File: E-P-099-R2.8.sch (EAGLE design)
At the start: 86 parts, among them J1 AVR_ISP

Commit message: pinouts updated to match new light boards
New changes to the pinouts for the ethernet connectors to match the new design of the head and tail light boards. Also designed to be symmetric across the connector to prevent mistakes.
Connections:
- removed net N$20: FRONT.1, U$20.D
- removed net N$23: FRONT.3, U$11.D
- new net N$14: FRONT.2, U$20.D
- new net N$15: FRONT.7, U$11.D
- net +12V: now also FRONT.3, FRONT.6, REAR.4, REAR.6; no longer FRONT.2, FRONT.7, REAR.1, REAR.2
- net N$27: now also FRONT.1; no longer FRONT.6
- net N$4: now also REAR.1; no longer REAR.7
- net N$43: now also REAR.7; no longer REAR.4
- net N$5: now also REAR.2; no longer REAR.6
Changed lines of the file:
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@@
 <instance part="R8" gate="G$1" x="111.76" y="226.06" rot="R90"/>
 <instance part="LED12" gate="G$1" x="111.76" y="236.22"/>
-<instance part="P+2" gate="1" x="45.72" y="27.94" rot="R180"/>
+<instance part="P+2" gate="1" x="43.18" y="27.94" rot="R180"/>
 <instance part="U$1" gate="G$1" x="408.94" y="144.78" rot="R90"/>
 <instance part="U$2" gate="G$1" x="391.16" y="129.54" rot="MR0"/>
@@
 <segment>
 <pinref part="P+6" gate="1" pin="+12V"/>
-<wire x1="53.34" y1="266.7" x2="53.34" y2="259.08" width="0.1524" layer="91"/>
-<wire x1="53.34" y1="259.08" x2="53.34" y2="254" width="0.1524" layer="91"/>
-<wire x1="53.34" y1="254" x2="53.34" y2="251.46" width="0.1524" layer="91"/>
-<wire x1="53.34" y1="251.46" x2="53.34" y2="246.38" width="0.1524" layer="91"/>
-<wire x1="53.34" y1="246.38" x2="60.96" y2="246.38" width="0.1524" layer="91"/>
-<wire x1="60.96" y1="251.46" x2="53.34" y2="251.46" width="0.1524" layer="91"/>
-<junction x="53.34" y="251.46"/>
-<wire x1="53.34" y1="254" x2="60.96" y2="254" width="0.1524" layer="91"/>
-<junction x="53.34" y="254"/>
-<wire x1="53.34" y1="259.08" x2="60.96" y2="259.08" width="0.1524" layer="91"/>
-<junction x="53.34" y="259.08"/>
-<pinref part="FRONT" gate="G$1" pin="2"/>
+<wire x1="53.34" y1="266.7" x2="53.34" y2="256.54" width="0.1524" layer="91"/>
+<pinref part="FRONT" gate="G$1" pin="6"/>
+<pinref part="FRONT" gate="G$1" pin="5"/>
+<wire x1="60.96" y1="248.92" x2="60.96" y2="251.46" width="0.1524" layer="91"/>
 <pinref part="FRONT" gate="G$1" pin="4"/>
-<pinref part="FRONT" gate="G$1" pin="5"/>
-<pinref part="FRONT" gate="G$1" pin="7"/>
-</segment>
-<segment>
+<wire x1="60.96" y1="251.46" x2="60.96" y2="254" width="0.1524" layer="91"/>
+<junction x="60.96" y="251.46"/>
+<pinref part="FRONT" gate="G$1" pin="3"/>
+<wire x1="60.96" y1="254" x2="60.96" y2="256.54" width="0.1524" layer="91"/>
+<junction x="60.96" y="254"/>
+<wire x1="60.96" y1="256.54" x2="53.34" y2="256.54" width="0.1524" layer="91"/>
+<junction x="60.96" y="256.54"/>
+</segment>
+<segment>
+<pinref part="REAR" gate="G$1" pin="6"/>
+<pinref part="REAR" gate="G$1" pin="5"/>
+<wire x1="43.18" y1="45.72" x2="43.18" y2="43.18" width="0.1524" layer="91"/>
+<pinref part="REAR" gate="G$1" pin="4"/>
+<wire x1="43.18" y1="43.18" x2="43.18" y2="40.64" width="0.1524" layer="91"/>
+<junction x="43.18" y="43.18"/>
+<pinref part="REAR" gate="G$1" pin="3"/>
+<wire x1="43.18" y1="40.64" x2="43.18" y2="38.1" width="0.1524" layer="91"/>
+<junction x="43.18" y="40.64"/>
+<wire x1="43.18" y1="38.1" x2="43.18" y2="30.48" width="0.1524" layer="91"/>
+<junction x="43.18" y="38.1"/>
 <pinref part="P+2" gate="1" pin="+12V"/>
-<wire x1="45.72" y1="30.48" x2="45.72" y2="33.02" width="0.1524" layer="91"/>
-<wire x1="45.72" y1="33.02" x2="45.72" y2="35.56" width="0.1524" layer="91"/>
-<wire x1="45.72" y1="35.56" x2="45.72" y2="38.1" width="0.1524" layer="91"/>
-<pinref part="REAR" gate="G$1" pin="3"/>
-<wire x1="43.18" y1="38.1" x2="45.72" y2="38.1" width="0.1524" layer="91"/>
-<pinref part="REAR" gate="G$1" pin="2"/>
-<wire x1="43.18" y1="35.56" x2="45.72" y2="35.56" width="0.1524" layer="91"/>
-<junction x="45.72" y="35.56"/>
-<pinref part="REAR" gate="G$1" pin="1"/>
-<wire x1="43.18" y1="33.02" x2="45.72" y2="33.02" width="0.1524" layer="91"/>
-<junction x="45.72" y="33.02"/>
-<wire x1="45.72" y1="38.1" x2="45.72" y2="43.18" width="0.1524" layer="91"/>
-<junction x="45.72" y="38.1"/>
-<pinref part="REAR" gate="G$1" pin="5"/>
-<wire x1="45.72" y1="43.18" x2="43.18" y2="43.18" width="0.1524" layer="91"/>
 </segment>
 </net>
 <net name="N$43" class="0">
 <segment>
-<wire x1="91.44" y1="40.64" x2="91.44" y2="60.96" width="0.1524" layer="91"/>
+<wire x1="91.44" y1="48.26" x2="91.44" y2="60.96" width="0.1524" layer="91"/>
 <wire x1="91.44" y1="60.96" x2="119.38" y2="60.96" width="0.1524" layer="91"/>
 <wire x1="119.38" y1="60.96" x2="119.38" y2="55.88" width="0.1524" layer="91"/>
 <pinref part="U$14" gate="G$1" pin="D"/>
-<pinref part="REAR" gate="G$1" pin="4"/>
-<wire x1="43.18" y1="40.64" x2="91.44" y2="40.64" width="0.1524" layer="91"/>
+<pinref part="REAR" gate="G$1" pin="7"/>
+<wire x1="43.18" y1="48.26" x2="91.44" y2="48.26" width="0.1524" layer="91"/>
 </segment>
 </net>
@@
 </segment>
 </net>
-<net name="N$20" class="0">
-<segment>
-<wire x1="40.64" y1="256.54" x2="40.64" y2="261.62" width="0.1524" layer="91"/>
-<wire x1="40.64" y1="261.62" x2="60.96" y2="261.62" width="0.1524" layer="91"/>
-<pinref part="U$20" gate="G$1" pin="D"/>
-<pinref part="FRONT" gate="G$1" pin="1"/>
-</segment>
-</net>
-<net name="N$23" class="0">
-<segment>
-<wire x1="45.72" y1="248.92" x2="45.72" y2="256.54" width="0.1524" layer="91"/>
-<wire x1="45.72" y1="256.54" x2="60.96" y2="256.54" width="0.1524" layer="91"/>
-<pinref part="U$11" gate="G$1" pin="D"/>
-<pinref part="FRONT" gate="G$1" pin="3"/>
-</segment>
-</net>
 <net name="N$27" class="0">
 <segment>
 <wire x1="50.8" y1="228.6" x2="50.8" y2="243.84" width="0.1524" layer="91"/>
 <wire x1="50.8" y1="243.84" x2="60.96" y2="243.84" width="0.1524" layer="91"/>
-<wire x1="50.8" y1="243.84" x2="50.8" y2="248.92" width="0.1524" layer="91"/>
+<pinref part="U$10" gate="G$1" pin="D"/>
+<pinref part="FRONT" gate="G$1" pin="8"/>
+<wire x1="50.8" y1="243.84" x2="50.8" y2="261.62" width="0.1524" layer="91"/>
 <junction x="50.8" y="243.84"/>
-<wire x1="50.8" y1="248.92" x2="60.96" y2="248.92" width="0.1524" layer="91"/>
-<pinref part="U$10" gate="G$1" pin="D"/>
-<pinref part="FRONT" gate="G$1" pin="6"/>
-<pinref part="FRONT" gate="G$1" pin="8"/>
+<pinref part="FRONT" gate="G$1" pin="1"/>
+<wire x1="50.8" y1="261.62" x2="60.96" y2="261.62" width="0.1524" layer="91"/>
 </segment>
 </net>
@@
 <net name="N$4" class="0">
 <segment>
-<pinref part="REAR" gate="G$1" pin="7"/>
-<pinref part="REAR" gate="G$1" pin="8"/>
-<wire x1="43.18" y1="48.26" x2="43.18" y2="50.8" width="0.1524" layer="91"/>
 <pinref part="U$13" gate="G$1" pin="D"/>
 <wire x1="58.42" y1="81.28" x2="93.98" y2="81.28" width="0.1524" layer="91"/>
+<wire x1="58.42" y1="81.28" x2="58.42" y2="50.8" width="0.1524" layer="91"/>
+<pinref part="REAR" gate="G$1" pin="1"/>
+<wire x1="58.42" y1="50.8" x2="58.42" y2="33.02" width="0.1524" layer="91"/>
+<wire x1="58.42" y1="33.02" x2="43.18" y2="33.02" width="0.1524" layer="91"/>
+<pinref part="REAR" gate="G$1" pin="8"/>
 <wire x1="43.18" y1="50.8" x2="58.42" y2="50.8" width="0.1524" layer="91"/>
-<wire x1="58.42" y1="50.8" x2="58.42" y2="81.28" width="0.1524" layer="91"/>
-<junction x="43.18" y="50.8"/>
+<junction x="58.42" y="50.8"/>
 </segment>
 </net>
@@
 <segment>
 <pinref part="U$15" gate="G$1" pin="D"/>
-<wire x1="119.38" y1="25.4" x2="119.38" y2="30.48" width="0.1524" layer="91"/>
-<pinref part="REAR" gate="G$1" pin="6"/>
-<wire x1="43.18" y1="45.72" x2="58.42" y2="45.72" width="0.1524" layer="91"/>
-<wire x1="58.42" y1="45.72" x2="58.42" y2="25.4" width="0.1524" layer="91"/>
-<wire x1="58.42" y1="25.4" x2="119.38" y2="25.4" width="0.1524" layer="91"/>
+<pinref part="REAR" gate="G$1" pin="2"/>
+<wire x1="43.18" y1="35.56" x2="101.6" y2="35.56" width="0.1524" layer="91"/>
+<wire x1="101.6" y1="35.56" x2="101.6" y2="30.48" width="0.1524" layer="91"/>
+<wire x1="101.6" y1="30.48" x2="119.38" y2="30.48" width="0.1524" layer="91"/>
 </segment>
 </net>
@@
 </segment>
 </net>
+<net name="N$14" class="0">
+<segment>
+<pinref part="U$20" gate="G$1" pin="D"/>
+<wire x1="40.64" y1="256.54" x2="40.64" y2="259.08" width="0.1524" layer="91"/>
+<pinref part="FRONT" gate="G$1" pin="2"/>
+<wire x1="40.64" y1="259.08" x2="60.96" y2="259.08" width="0.1524" layer="91"/>
+</segment>
+</net>
+<net name="N$15" class="0">
+<segment>
+<pinref part="U$11" gate="G$1" pin="D"/>
+<wire x1="45.72" y1="248.92" x2="55.88" y2="248.92" width="0.1524" layer="91"/>
+<wire x1="55.88" y1="248.92" x2="55.88" y2="246.38" width="0.1524" layer="91"/>
+<pinref part="FRONT" gate="G$1" pin="7"/>
+<wire x1="55.88" y1="246.38" x2="60.96" y2="246.38" width="0.1524" layer="91"/>
+</segment>
+</net>

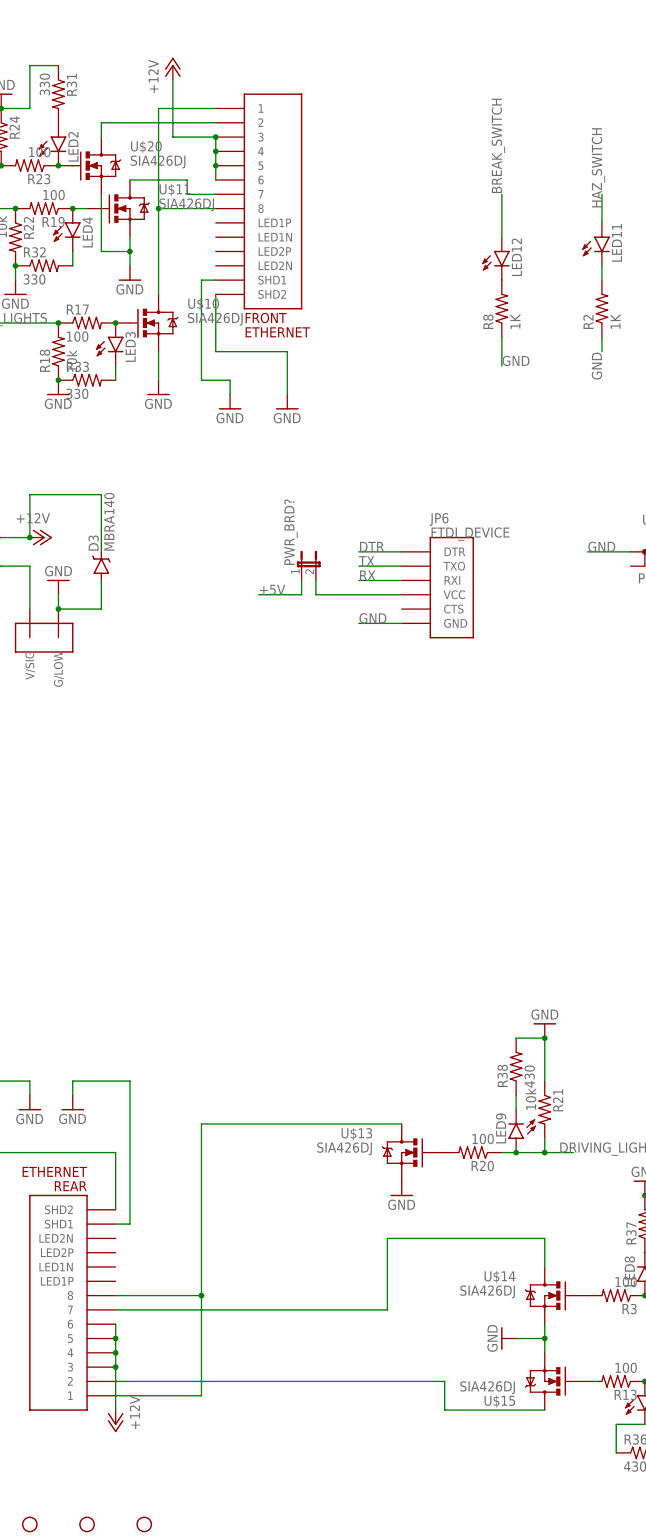
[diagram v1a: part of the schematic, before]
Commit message: Revert "pinouts updated to match new light boards"
This reverts commit c6705fe930e627c4a8d5c034fe7450b97c4f4bb6.
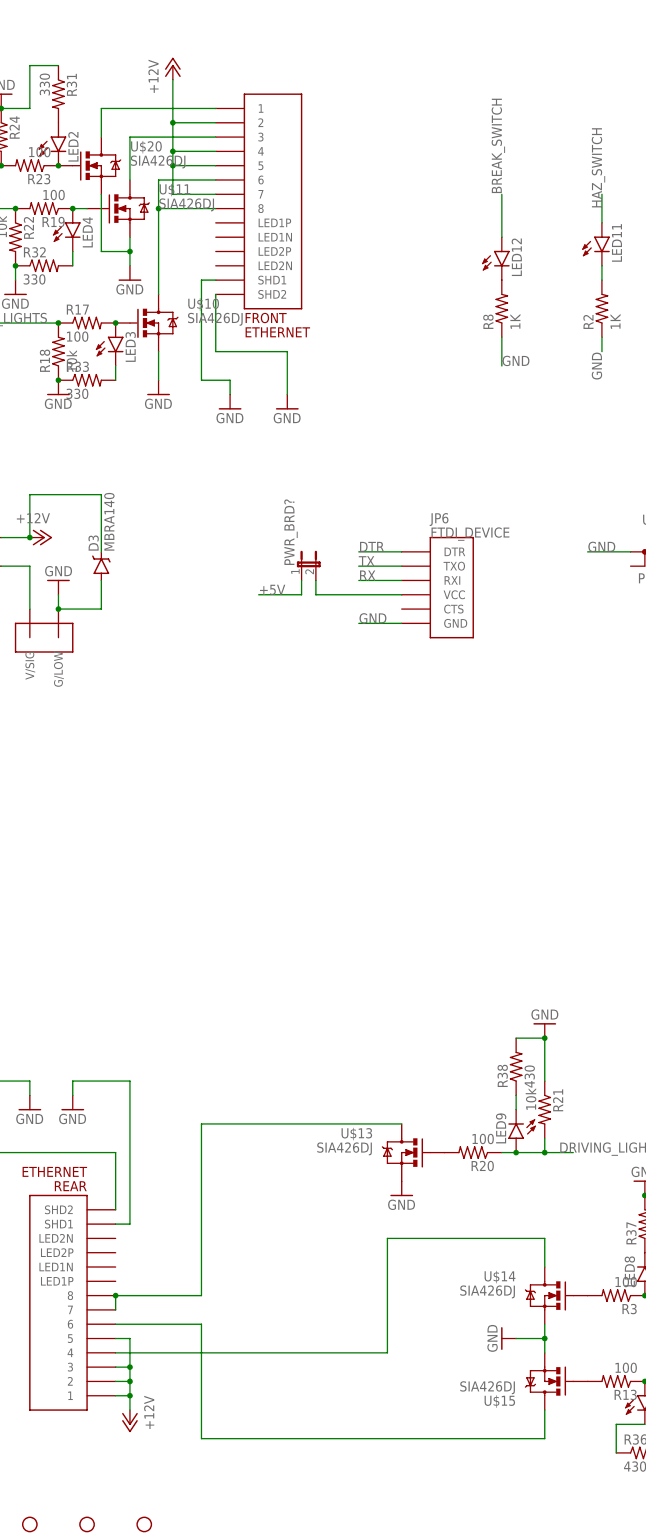
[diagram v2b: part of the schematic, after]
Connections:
- removed net N$14: FRONT.2, U$20.D
- removed net N$15: FRONT.7, U$11.D
- new net N$20: FRONT.1, U$20.D
- new net N$23: FRONT.3, U$11.D
- net +12V: now also FRONT.2, FRONT.7, REAR.1, REAR.2; no longer FRONT.3, FRONT.6, REAR.4, REAR.6
- net N$27: now also FRONT.6; no longer FRONT.1
- net N$4: now also REAR.7; no longer REAR.1
- net N$43: now also REAR.4; no longer REAR.7
- net N$5: now also REAR.6; no longer REAR.2
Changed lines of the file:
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@@
 <instance part="R8" gate="G$1" x="111.76" y="226.06" rot="R90"/>
 <instance part="LED12" gate="G$1" x="111.76" y="236.22"/>
-<instance part="P+2" gate="1" x="43.18" y="27.94" rot="R180"/>
+<instance part="P+2" gate="1" x="45.72" y="27.94" rot="R180"/>
 <instance part="U$1" gate="G$1" x="408.94" y="144.78" rot="R90"/>
 <instance part="U$2" gate="G$1" x="391.16" y="129.54" rot="MR0"/>
@@
 <segment>
 <pinref part="P+6" gate="1" pin="+12V"/>
-<wire x1="53.34" y1="266.7" x2="53.34" y2="256.54" width="0.1524" layer="91"/>
-<pinref part="FRONT" gate="G$1" pin="6"/>
+<wire x1="53.34" y1="266.7" x2="53.34" y2="259.08" width="0.1524" layer="91"/>
+<wire x1="53.34" y1="259.08" x2="53.34" y2="254" width="0.1524" layer="91"/>
+<wire x1="53.34" y1="254" x2="53.34" y2="251.46" width="0.1524" layer="91"/>
+<wire x1="53.34" y1="251.46" x2="53.34" y2="246.38" width="0.1524" layer="91"/>
+<wire x1="53.34" y1="246.38" x2="60.96" y2="246.38" width="0.1524" layer="91"/>
+<wire x1="60.96" y1="251.46" x2="53.34" y2="251.46" width="0.1524" layer="91"/>
+<junction x="53.34" y="251.46"/>
+<wire x1="53.34" y1="254" x2="60.96" y2="254" width="0.1524" layer="91"/>
+<junction x="53.34" y="254"/>
+<wire x1="53.34" y1="259.08" x2="60.96" y2="259.08" width="0.1524" layer="91"/>
+<junction x="53.34" y="259.08"/>
+<pinref part="FRONT" gate="G$1" pin="2"/>
+<pinref part="FRONT" gate="G$1" pin="4"/>
 <pinref part="FRONT" gate="G$1" pin="5"/>
-<wire x1="60.96" y1="248.92" x2="60.96" y2="251.46" width="0.1524" layer="91"/>
-<pinref part="FRONT" gate="G$1" pin="4"/>
-<wire x1="60.96" y1="251.46" x2="60.96" y2="254" width="0.1524" layer="91"/>
-<junction x="60.96" y="251.46"/>
-<pinref part="FRONT" gate="G$1" pin="3"/>
-<wire x1="60.96" y1="254" x2="60.96" y2="256.54" width="0.1524" layer="91"/>
-<junction x="60.96" y="254"/>
-<wire x1="60.96" y1="256.54" x2="53.34" y2="256.54" width="0.1524" layer="91"/>
-<junction x="60.96" y="256.54"/>
-</segment>
-<segment>
-<pinref part="REAR" gate="G$1" pin="6"/>
+<pinref part="FRONT" gate="G$1" pin="7"/>
+</segment>
+<segment>
+<pinref part="P+2" gate="1" pin="+12V"/>
+<wire x1="45.72" y1="30.48" x2="45.72" y2="33.02" width="0.1524" layer="91"/>
+<wire x1="45.72" y1="33.02" x2="45.72" y2="35.56" width="0.1524" layer="91"/>
+<wire x1="45.72" y1="35.56" x2="45.72" y2="38.1" width="0.1524" layer="91"/>
+<pinref part="REAR" gate="G$1" pin="3"/>
+<wire x1="43.18" y1="38.1" x2="45.72" y2="38.1" width="0.1524" layer="91"/>
+<pinref part="REAR" gate="G$1" pin="2"/>
+<wire x1="43.18" y1="35.56" x2="45.72" y2="35.56" width="0.1524" layer="91"/>
+<junction x="45.72" y="35.56"/>
+<pinref part="REAR" gate="G$1" pin="1"/>
+<wire x1="43.18" y1="33.02" x2="45.72" y2="33.02" width="0.1524" layer="91"/>
+<junction x="45.72" y="33.02"/>
+<wire x1="45.72" y1="38.1" x2="45.72" y2="43.18" width="0.1524" layer="91"/>
+<junction x="45.72" y="38.1"/>
 <pinref part="REAR" gate="G$1" pin="5"/>
-<wire x1="43.18" y1="45.72" x2="43.18" y2="43.18" width="0.1524" layer="91"/>
-<pinref part="REAR" gate="G$1" pin="4"/>
-<wire x1="43.18" y1="43.18" x2="43.18" y2="40.64" width="0.1524" layer="91"/>
-<junction x="43.18" y="43.18"/>
-<pinref part="REAR" gate="G$1" pin="3"/>
-<wire x1="43.18" y1="40.64" x2="43.18" y2="38.1" width="0.1524" layer="91"/>
-<junction x="43.18" y="40.64"/>
-<wire x1="43.18" y1="38.1" x2="43.18" y2="30.48" width="0.1524" layer="91"/>
-<junction x="43.18" y="38.1"/>
-<pinref part="P+2" gate="1" pin="+12V"/>
+<wire x1="45.72" y1="43.18" x2="43.18" y2="43.18" width="0.1524" layer="91"/>
 </segment>
 </net>
 <net name="N$43" class="0">
 <segment>
-<wire x1="91.44" y1="48.26" x2="91.44" y2="60.96" width="0.1524" layer="91"/>
+<wire x1="91.44" y1="40.64" x2="91.44" y2="60.96" width="0.1524" layer="91"/>
 <wire x1="91.44" y1="60.96" x2="119.38" y2="60.96" width="0.1524" layer="91"/>
 <wire x1="119.38" y1="60.96" x2="119.38" y2="55.88" width="0.1524" layer="91"/>
 <pinref part="U$14" gate="G$1" pin="D"/>
-<pinref part="REAR" gate="G$1" pin="7"/>
-<wire x1="43.18" y1="48.26" x2="91.44" y2="48.26" width="0.1524" layer="91"/>
+<pinref part="REAR" gate="G$1" pin="4"/>
+<wire x1="43.18" y1="40.64" x2="91.44" y2="40.64" width="0.1524" layer="91"/>
 </segment>
 </net>
@@
 </segment>
 </net>
+<net name="N$20" class="0">
+<segment>
+<wire x1="40.64" y1="256.54" x2="40.64" y2="261.62" width="0.1524" layer="91"/>
+<wire x1="40.64" y1="261.62" x2="60.96" y2="261.62" width="0.1524" layer="91"/>
+<pinref part="U$20" gate="G$1" pin="D"/>
+<pinref part="FRONT" gate="G$1" pin="1"/>
+</segment>
+</net>
+<net name="N$23" class="0">
+<segment>
+<wire x1="45.72" y1="248.92" x2="45.72" y2="256.54" width="0.1524" layer="91"/>
+<wire x1="45.72" y1="256.54" x2="60.96" y2="256.54" width="0.1524" layer="91"/>
+<pinref part="U$11" gate="G$1" pin="D"/>
+<pinref part="FRONT" gate="G$1" pin="3"/>
+</segment>
+</net>
 <net name="N$27" class="0">
 <segment>
 <wire x1="50.8" y1="228.6" x2="50.8" y2="243.84" width="0.1524" layer="91"/>
 <wire x1="50.8" y1="243.84" x2="60.96" y2="243.84" width="0.1524" layer="91"/>
+<wire x1="50.8" y1="243.84" x2="50.8" y2="248.92" width="0.1524" layer="91"/>
+<junction x="50.8" y="243.84"/>
+<wire x1="50.8" y1="248.92" x2="60.96" y2="248.92" width="0.1524" layer="91"/>
 <pinref part="U$10" gate="G$1" pin="D"/>
+<pinref part="FRONT" gate="G$1" pin="6"/>
 <pinref part="FRONT" gate="G$1" pin="8"/>
-<wire x1="50.8" y1="243.84" x2="50.8" y2="261.62" width="0.1524" layer="91"/>
-<junction x="50.8" y="243.84"/>
-<pinref part="FRONT" gate="G$1" pin="1"/>
-<wire x1="50.8" y1="261.62" x2="60.96" y2="261.62" width="0.1524" layer="91"/>
 </segment>
 </net>
@@
 <net name="N$4" class="0">
 <segment>
+<pinref part="REAR" gate="G$1" pin="7"/>
+<pinref part="REAR" gate="G$1" pin="8"/>
+<wire x1="43.18" y1="48.26" x2="43.18" y2="50.8" width="0.1524" layer="91"/>
 <pinref part="U$13" gate="G$1" pin="D"/>
 <wire x1="58.42" y1="81.28" x2="93.98" y2="81.28" width="0.1524" layer="91"/>
-<wire x1="58.42" y1="81.28" x2="58.42" y2="50.8" width="0.1524" layer="91"/>
-<pinref part="REAR" gate="G$1" pin="1"/>
-<wire x1="58.42" y1="50.8" x2="58.42" y2="33.02" width="0.1524" layer="91"/>
-<wire x1="58.42" y1="33.02" x2="43.18" y2="33.02" width="0.1524" layer="91"/>
-<pinref part="REAR" gate="G$1" pin="8"/>
 <wire x1="43.18" y1="50.8" x2="58.42" y2="50.8" width="0.1524" layer="91"/>
-<junction x="58.42" y="50.8"/>
+<wire x1="58.42" y1="50.8" x2="58.42" y2="81.28" width="0.1524" layer="91"/>
+<junction x="43.18" y="50.8"/>
 </segment>
 </net>
@@
 <segment>
 <pinref part="U$15" gate="G$1" pin="D"/>
-<pinref part="REAR" gate="G$1" pin="2"/>
-<wire x1="43.18" y1="35.56" x2="101.6" y2="35.56" width="0.1524" layer="91"/>
-<wire x1="101.6" y1="35.56" x2="101.6" y2="30.48" width="0.1524" layer="91"/>
-<wire x1="101.6" y1="30.48" x2="119.38" y2="30.48" width="0.1524" layer="91"/>
+<wire x1="119.38" y1="25.4" x2="119.38" y2="30.48" width="0.1524" layer="91"/>
+<pinref part="REAR" gate="G$1" pin="6"/>
+<wire x1="43.18" y1="45.72" x2="58.42" y2="45.72" width="0.1524" layer="91"/>
+<wire x1="58.42" y1="45.72" x2="58.42" y2="25.4" width="0.1524" layer="91"/>
+<wire x1="58.42" y1="25.4" x2="119.38" y2="25.4" width="0.1524" layer="91"/>
 </segment>
 </net>
@@
 </segment>
 </net>
-<net name="N$14" class="0">
-<segment>
-<pinref part="U$20" gate="G$1" pin="D"/>
-<wire x1="40.64" y1="256.54" x2="40.64" y2="259.08" width="0.1524" layer="91"/>
-<pinref part="FRONT" gate="G$1" pin="2"/>
-<wire x1="40.64" y1="259.08" x2="60.96" y2="259.08" width="0.1524" layer="91"/>
-</segment>
-</net>
-<net name="N$15" class="0">
-<segment>
-<pinref part="U$11" gate="G$1" pin="D"/>
-<wire x1="45.72" y1="248.92" x2="55.88" y2="248.92" width="0.1524" layer="91"/>
-<wire x1="55.88" y1="248.92" x2="55.88" y2="246.38" width="0.1524" layer="91"/>
-<pinref part="FRONT" gate="G$1" pin="7"/>
-<wire x1="55.88" y1="246.38" x2="60.96" y2="246.38" width="0.1524" layer="91"/>
-</segment>
-</net>
